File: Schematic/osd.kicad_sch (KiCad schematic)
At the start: 12 parts, among them U9 AT7456E, Y2 Crystal

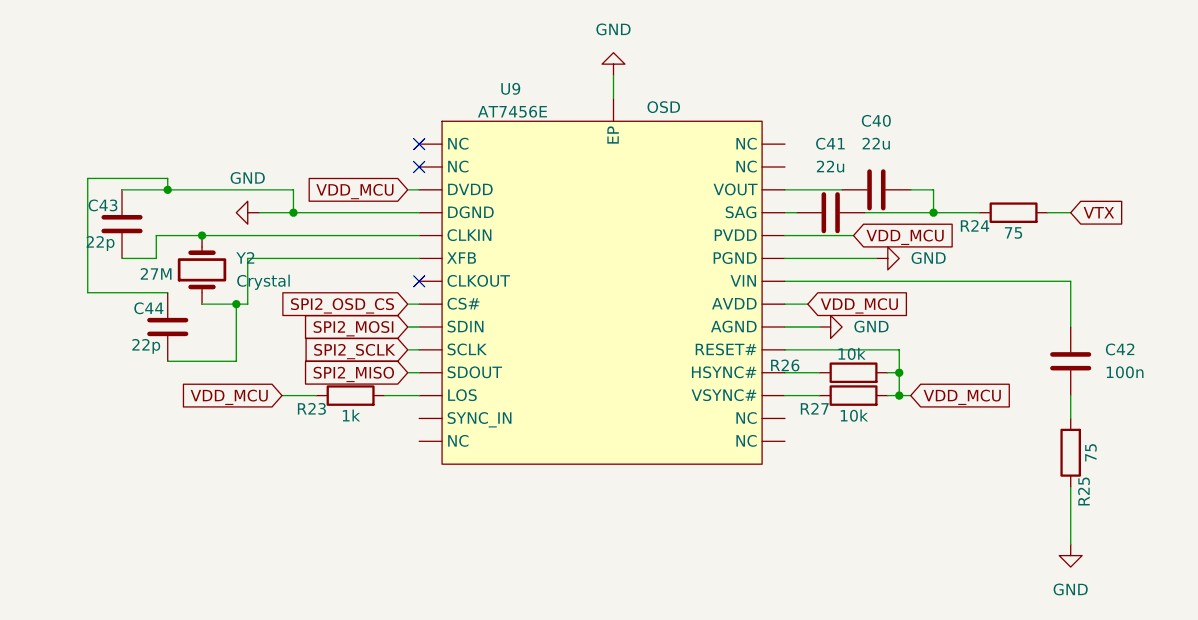
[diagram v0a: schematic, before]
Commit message: schematic fully finished, every footprint assigned, still electrical checking to do
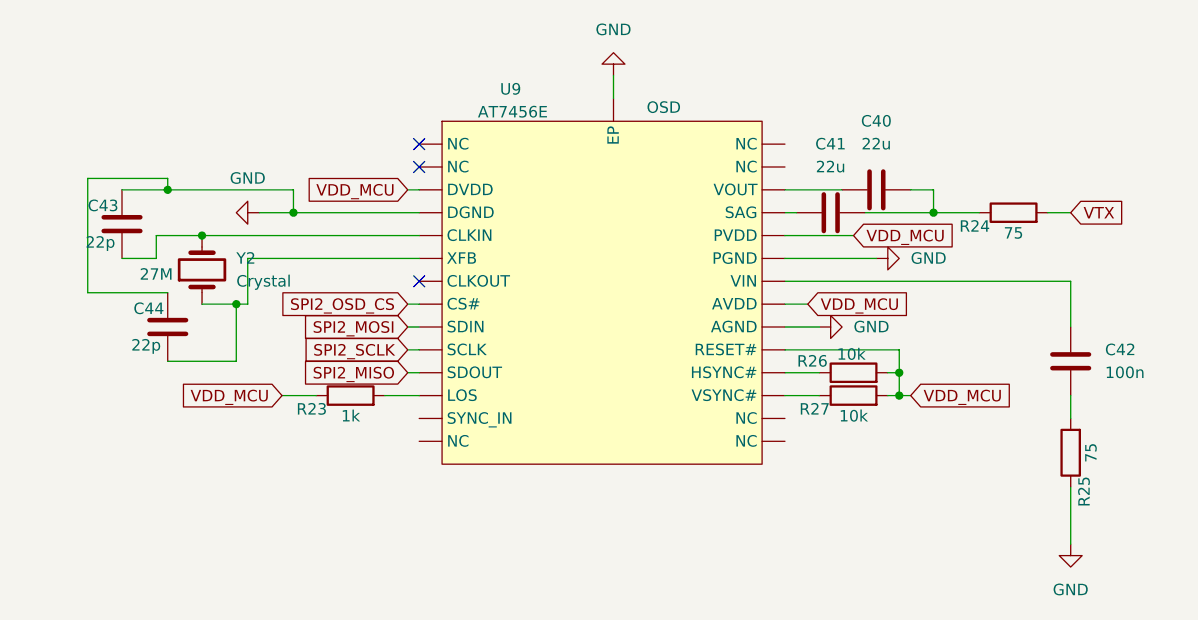
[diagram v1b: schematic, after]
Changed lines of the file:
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@@
 		(dnp no)
 		(property "Reference" "R26"
-			(at 119.38 75.438 90)
+			(at 122.428 74.93 90)
 			(effects
 				(font

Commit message: reviewing and refactoring footprints and full schematic
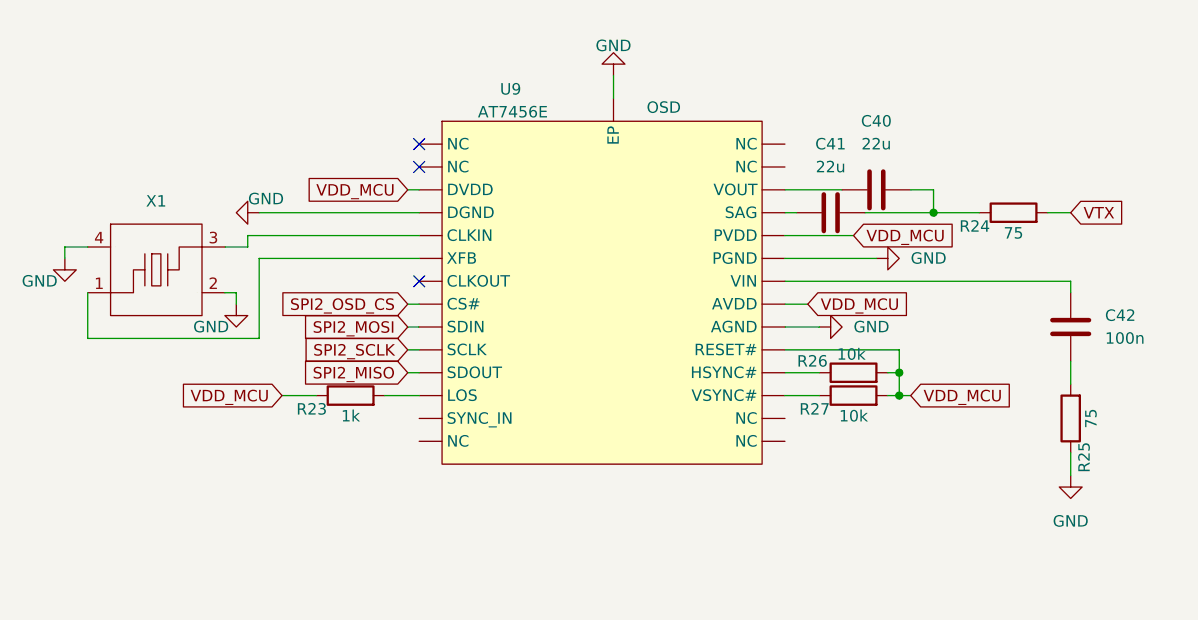
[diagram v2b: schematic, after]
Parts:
- removed C43, C44: 22p, Capacitor_SMD:C_0603_1608Metric, symbol Device:C
- removed Y2: Crystal, Crystal:Crystal_SMD_3225-4Pin_3.2x2.5mm, symbol Device:Crystal
- added X1: 27MHz, fch7_fp:CRYSTAL-SMD_4P-L2.0-W1.6-BL, symbol fch7_sym:XL7EL89COI-111YLC-27M
- C40, C41: footprint Capacitor_SMD:C_1210_3225Metric -> Capacitor_SMD:C_0805_2012Metric; MPN (none) -> CL21A226MAQNNNE; Manufacturer (none) -> SAMSUNG
- C42: MPN (none) -> 0603B104K500NT; Manufacturer (none) -> FH
- R23: MPN (none) -> RC0603FR-071KL; Manufacturer (none) -> YAGEO
- R24, R25: MPN (none) -> 0603WAF750JT5E; Manufacturer (none) -> UNI-ROYAL
- R26, R27: MPN (none) -> 0603WAF1002T5E; Manufacturer (none) -> UNI-ROYAL
- U9: MPN (none) -> AT7456E; Manufacturer (none) -> ZHONGKEWEI
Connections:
- net GND: now also X1.2 (GND), X1.4 (GND)
- new net: U9. (NC), X1.1
- new net: U9. (NC), X1.3
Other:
- moved on the sheet: C42, R25

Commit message: Update schematic and footprint libraries with various component modifications
- Updated fp-info-cache with new component details and footprint changes.
- Modified osd.kicad_sch to correct pin types and add no_connect entries.
- Adjusted rf_rx.kicad_sch to fix pin assignments and update component properties.
- Enhanced sensors.kicad_sch with new properties for QMC5883L and SPL06-001 sensors.
- Added new libraries to sym-lib-table and fp-lib-table for better organization and access to components.
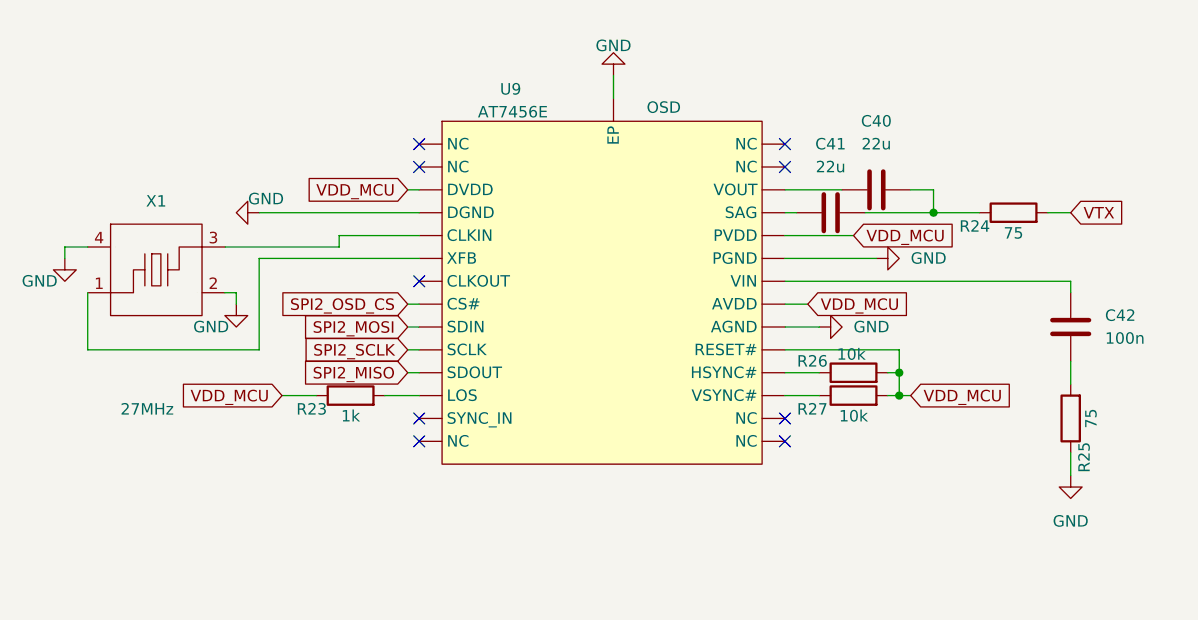
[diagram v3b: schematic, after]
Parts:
- X1: footprint fch7_fp:CRYSTAL-SMD_4P-L2.0-W1.6-BL -> ProLib_pcs_2025-11-25:CRYSTAL-SMD_4P-L2.0-W1.6-BL; Manufacturer YXC Crystal Oscillators -> YXC(扬兴晶振)
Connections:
- no-connect marks 3 -> 9
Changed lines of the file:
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@@
+	)
+	(no_connect
+		(at 119.38 53.34)
 	)
 	(no_connect
@@
 		(at 78.74 50.8)
 	)
+	(no_connect
+		(at 119.38 83.82)
+	)
+	(no_connect
+		(at 78.74 81.28)
+	)
+	(no_connect
+		(at 119.38 50.8)
+	)
+	(no_connect
+		(at 119.38 81.28)
+	)
+	(no_connect
+		(at 78.74 83.82)
+	)
+	(wire
+		(pts
+			(xy 57.15 62.23) (xy 69.85 62.23)
+		)
+		(stroke
+			(width 0)
+			(type default)
+		)
+	)
 	(wire
 		(pts
@@
 	(wire
 		(pts
-			(xy 59.69 62.23) (xy 57.15 62.23)
-		)
-		(stroke
-			(width 0)
-			(type default)
-		)
-	)
-	(wire
-		(pts
 			(xy 58.42 67.31) (xy 57.15 67.31)
 		)
@@
 	(wire
 		(pts
-			(xy 60.96 63.5) (xy 60.96 72.39)
-		)
-		(stroke
-			(width 0)
-			(type default)
-		)
-	)
-	(wire
-		(pts
 			(xy 77.47 55.88) (xy 78.74 55.88)
 		)
@@
 	(wire
 		(pts
+			(xy 60.96 73.66) (xy 60.96 63.5)
+		)
+		(stroke
+			(width 0)
+			(type default)
+		)
+	)
+	(wire
+		(pts
 			(xy 74.93 78.74) (xy 78.74 78.74)
 		)
@@
 	(wire
 		(pts
-			(xy 78.74 60.96) (xy 59.69 60.96)
-		)
-		(stroke
-			(width 0)
-			(type default)
-		)
-	)
-	(wire
-		(pts
-			(xy 59.69 60.96) (xy 59.69 62.23)
+			(xy 69.85 60.96) (xy 78.74 60.96)
+		)
+		(stroke
+			(width 0)
+			(type default)
+		)
+	)
+	(wire
+		(pts
+			(xy 69.85 62.23) (xy 69.85 60.96)
 		)
 		(stroke
@@
 	(wire
 		(pts
+			(xy 41.91 67.31) (xy 41.91 73.66)
+		)
+		(stroke
+			(width 0)
+			(type default)
+		)
+	)
+	(wire
+		(pts
 			(xy 100.33 43.18) (xy 100.33 45.72)
 		)
@@
 	(wire
 		(pts
+			(xy 60.96 63.5) (xy 78.74 63.5)
+		)
+		(stroke
+			(width 0)
+			(type default)
+		)
+	)
+	(wire
+		(pts
 			(xy 119.38 76.2) (xy 123.19 76.2)
 		)
@@
 	(wire
 		(pts
-			(xy 41.91 72.39) (xy 60.96 72.39)
-		)
-		(stroke
-			(width 0)
-			(type default)
-		)
-	)
-	(wire
-		(pts
 			(xy 133.35 55.88) (xy 135.89 55.88)
 		)
@@
 	(wire
 		(pts
+			(xy 41.91 73.66) (xy 60.96 73.66)
+		)
+		(stroke
+			(width 0)
+			(type default)
+		)
+	)
+	(wire
+		(pts
 			(xy 63.5 78.74) (xy 67.31 78.74)
 		)
@@
 	(wire
 		(pts
-			(xy 78.74 63.5) (xy 60.96 63.5)
-		)
-		(stroke
-			(width 0)
-			(type default)
-		)
-	)
-	(wire
-		(pts
 			(xy 128.27 58.42) (xy 135.89 58.42)
-		)
-		(stroke
-			(width 0)
-			(type default)
-		)
-	)
-	(wire
-		(pts
-			(xy 41.91 72.39) (xy 41.91 67.31)
 		)
 		(stroke
@@
 					(size 1.27 1.27)
 				)
-				(hide yes)
-			)
-		)
-		(property "Footprint" "fch7_fp:CRYSTAL-SMD_4P-L2.0-W1.6-BL"
+			)
+		)
+		(property "Footprint" "ProLib_pcs_2025-11-25:CRYSTAL-SMD_4P-L2.0-W1.6-BL"
 			(at 50.546 54.356 0)
 			(effects
@@
 			)
 		)
-		(property "Datasheet" "https://www.lcsc.com/datasheet/C18214311.pdf"
+		(property "Datasheet" "https://item.szlcsc.com/datasheet/XL7EL89COI-111YLC-27M/19392660.html"
 			(at 50.038 70.612 0)
 			(effects
@@
 			)
 		)
-		(property "Manufacturer" "YXC Crystal Oscillators"
+		(property "Manufacturer" "YXC(扬兴晶振)"
 			(at 49.022 50.546 0)
 			(effects
@@
 		(dnp no)
 		(property "Reference" "R27"
-			(at 122.682 80.264 90)
-			(effects
-				(font
+			(at 122.428 80.264 90)
+			(effects
+				(font

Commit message: Refactor fp-lib-table: Remove unused libraries and update description for fch7_fp
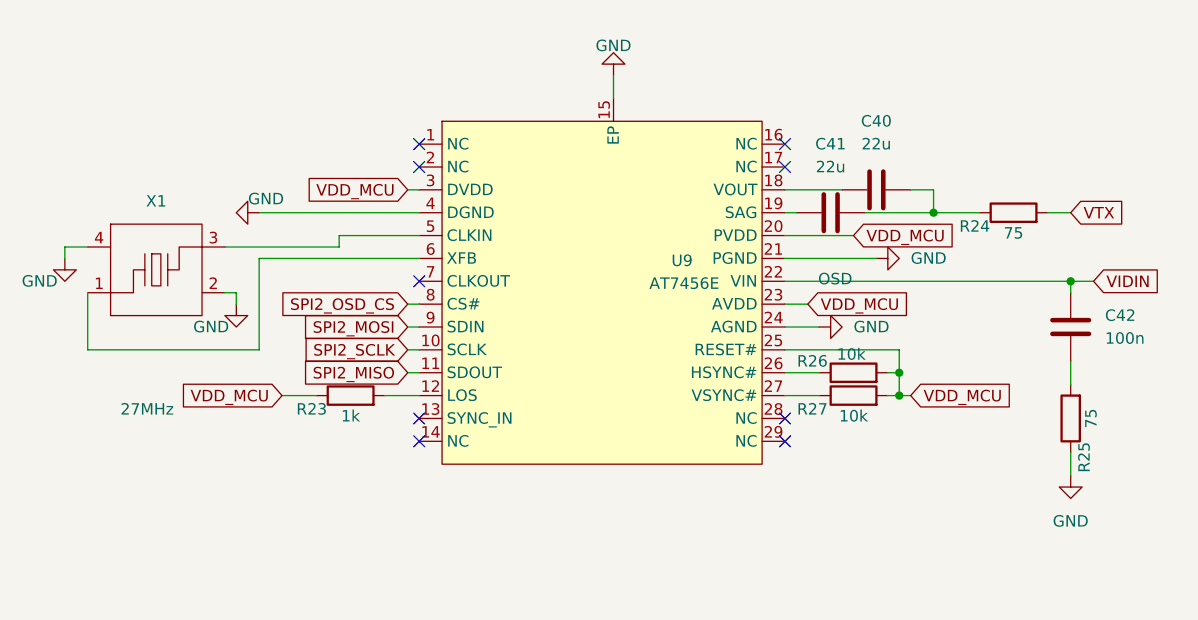
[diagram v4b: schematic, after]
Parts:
- X1: footprint ProLib_pcs_2025-11-25:CRYSTAL-SMD_4P-L2.0-W1.6-BL -> fch7_fp:CRYSTAL-SMD_4P-L2.0-W1.6-BL
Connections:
- net GND: now also U9.15 (EP), U9.21 (PGND), U9.24 (AGND), U9.4 (DGND); no longer U9. (NC)
- net SPI2_MISO: now also U9.11 (SDOUT); no longer U9. (NC)
- net SPI2_MOSI: now also U9.9 (SDIN); no longer U9. (NC)
- net SPI2_OSD_CS: now also U9.8 (CS#); no longer U9. (NC)
- net SPI2_SCLK: now also U9.10 (SCLK); no longer U9. (NC)
- net VDD_MCU: now also U9.20 (PVDD), U9.23 (AVDD), U9.25 (RESET#), U9.3 (DVDD); no longer U9. (NC)
- net at R23.2: now also U9.12 (LOS); no longer U9. (NC)
- net at X1.1: now also U9.6 (XFB); no longer U9. (NC)
- net at X1.3: now also U9.5 (CLKIN); no longer U9. (NC)
- net at R27.1: now also U9.27 (VSYNC#); no longer U9. (NC)
- net at C40.1: now also U9.18 (VOUT); no longer U9. (NC)
- net VIDIN: now reaches C42.2
- net VIDIN: now also U9.22 (VIN); no longer U9. (NC)
- net at R26.1: now also U9.26 (HSYNC#); no longer U9. (NC)
- net at C41.1: now also U9.19 (SAG); no longer U9. (NC)
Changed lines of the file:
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@@
+	)
+	(junction
+		(at 151.13 66.04)
+		(diameter 0)
+		(color 0 0 0 0)
 	)
 	(junction
@@
 		(pts
 			(xy 60.96 58.42) (xy 78.74 58.42)
+		)
+		(stroke
+			(width 0)
+			(type default)
+		)
+	)
+	(wire
+		(pts
+			(xy 151.13 66.04) (xy 153.67 66.04)
 		)
 		(stroke
@@
 				)
 				(justify right)
+				(hide yes)
+			)
+		)
+	)
+	(global_label "VIDIN"
+		(shape input)
+		(at 153.67 66.04 0)
+		(fields_autoplaced yes)
+		(effects
+			(font
+				(size 1.27 1.27)
+			)
+			(justify left)
+		)
+		(property "Intersheetrefs" "${INTERSHEET_REFS}"
+			(at 161.5539 66.04 0)
+			(effects
+				(font
+					(size 1.27 1.27)
+				)
+				(justify left)
 				(hide yes)
 			)
@@
 			)
 		)
-		(property "Footprint" "ProLib_pcs_2025-11-25:CRYSTAL-SMD_4P-L2.0-W1.6-BL"
+		(property "Footprint" "fch7_fp:CRYSTAL-SMD_4P-L2.0-W1.6-BL"
 			(at 50.546 54.356 0)
 			(effects
@@
 	(symbol
 		(lib_id "fclib:AT7456E")
-		(at 80.01 46.99 0)
+		(at 99.06 66.04 0)
 		(unit 1)
 		(exclude_from_sim no)
@@
 		(dnp no)
 		(property "Reference" "U9"
-			(at 88.9 44.704 0)
+			(at 107.95 63.754 0)
 			(effects
 				(font
@@
 		)
 		(property "Value" "AT7456E"
-			(at 89.154 47.244 0)
+			(at 108.204 66.294 0)
 			(effects
 				(font
@@
 		)
 		(property "Footprint" "fch7_fp:TSSOP-28_L9.7-W4.4-P0.65-LS6.4-BL-EP-2"
-			(at 80.01 46.99 0)
+			(at 99.06 66.04 0)
 			(effects
 				(font
@@
 		)
 		(property "Datasheet" "https://www.lcsc.com/datasheet/C82351.pdf"
-			(at 80.01 46.99 0)
+			(at 99.06 66.04 0)
 			(effects
 				(font
@@
 		)
 		(property "Description" "OSD"
-			(at 105.918 46.736 0)
+			(at 124.968 65.786 0)
 			(effects
 				(font
@@
 		)
 		(property "Fréquence" ""
-			(at 80.01 46.99 0)
+			(at 99.06 66.04 0)
 			(effects
 				(font
@@
 		)
 		(property "MPN" "AT7456E"
-			(at 80.01 46.99 0)
+			(at 99.06 66.04 0)
 			(effects
 				(font
@@
 		)
 		(property "Manufacturer" "ZHONGKEWEI"
-			(at 80.01 46.99 0)
-			(effects
-				(font
-					(size 1.27 1.27)
-				)
-				(hide yes)
-			)
-		)
-		(pin ""
-		)
-		(pin ""
-		)
-		(pin ""
-		)
-		(pin ""
-		)
-		(pin ""
-		)
-		(pin ""
-		)
-		(pin ""
-		)
-		(pin ""
-		)
-		(pin ""
-		)
-		(pin ""
-		)
-		(pin ""
-		)
-		(pin ""
-		)
-		(pin ""
-		)
-		(pin ""
-		)
-		(pin ""
-		)
-		(pin ""
-		)
-		(pin ""
-		)
-		(pin ""
-		)
-		(pin ""
-		)
-		(pin ""
-		)
-		(pin ""
-		)
-		(pin ""
-		)
-		(pin ""
-		)
-		(pin ""
-		)
-		(pin ""
-		)
-		(pin ""
-		)
-		(pin ""
-		)
-		(pin ""
-		)
-		(pin ""
+			(at 99.06 66.04 0)
+			(effects
+				(font
+					(size 1.27 1.27)
+				)
+				(hide yes)
+			)
+		)
+		(pin "10"
+		)
+		(pin "4"
+		)
+		(pin "9"
+		)
+		(pin "2"
+		)
+		(pin "11"
+		)
+		(pin "7"
+		)
+		(pin "13"
+		)
+		(pin "5"
+		)
+		(pin "12"
+		)
+		(pin "3"
+		)
+		(pin "6"
+		)
+		(pin "8"
+		)
+		(pin "1"
+		)
+		(pin "29"
+		)
+		(pin "16"
+		)
+		(pin "27"
+		)
+		(pin "20"
+		)
+		(pin "19"
+		)
+		(pin "14"
+		)
+		(pin "25"
+		)
+		(pin "23"
+		)
+		(pin "22"
+		)
+		(pin "28"
+		)
+		(pin "24"
+		)
+		(pin "21"
+		)
+		(pin "18"
+		)
+		(pin "26"
+		)
+		(pin "15"
+		)
+		(pin "17"
 		)
 		(instances

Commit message: Refactor schematic files and update component placements
- Adjusted component positions in osd.kicad_sch for better layout.
- Added new junctions and wires in rf_rx.kicad_sch to improve connectivity.
- Introduced additional junctions and wires in sensors.kicad_sch for enhanced signal routing.
- Removed outdated backup file fch7-2025-11-18_191836.zip and added new backup fch7-2025-11-27_202230.zip.
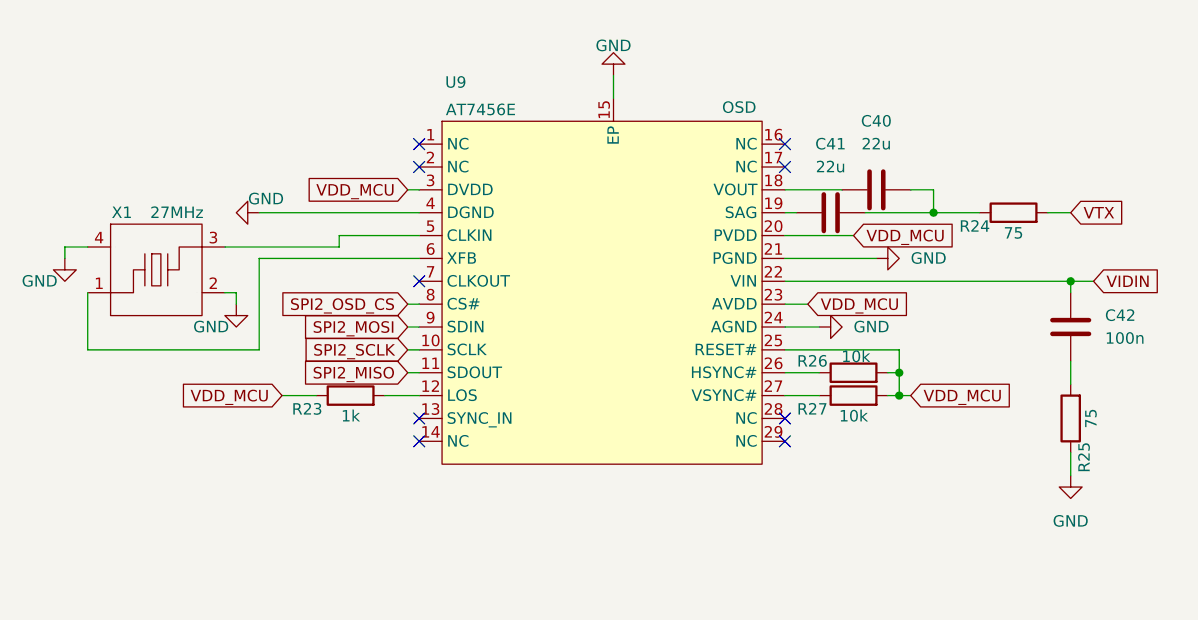
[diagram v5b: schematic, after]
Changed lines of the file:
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@@
 		(dnp no)
 		(property "Reference" "R23"
-			(at 66.802 80.264 90)
+			(at 66.294 80.264 90)
 			(effects
 				(font
@@
 		(on_board yes)
 		(dnp no)
-		(fields_autoplaced yes)
 		(property "Reference" "X1"
-			(at 49.53 57.15 0)
+			(at 45.72 58.42 0)
 			(effects
 				(font
@@
 		)
 		(property "Value" "27MHz"
-			(at 48.514 80.264 0)
+			(at 51.816 58.42 0)
 			(effects
 				(font
@@
 		(dnp no)
 		(property "Reference" "U9"
-			(at 107.95 63.754 0)
+			(at 82.804 43.942 0)
 			(effects
 				(font
@@
 		)
 		(property "Value" "AT7456E"
-			(at 108.204 66.294 0)
+			(at 85.598 46.99 0)
 			(effects
 				(font
@@
 		)
 		(property "Description" "OSD"
-			(at 124.968 65.786 0)
+			(at 114.3 46.736 0)
 			(effects
 				(font
@@
 		)
 		(property "Value" "10k"
-			(at 126.746 74.168 90)
-			(effects
-				(font
+			(at 127.254 74.422 90)
+			(effects
+				(font
